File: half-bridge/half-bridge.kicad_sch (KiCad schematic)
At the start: 97 parts, among them J1 Conn_01x11_Pin, J3 Conn_01x11_Pin, J4 Conn_01x11_Pin, J5 Conn_01x11_Pin, J6 Conn_01x11_Pin, Q1 EPC2306, Q2 EPC2306, U1 LMG1210, U2 INA293B

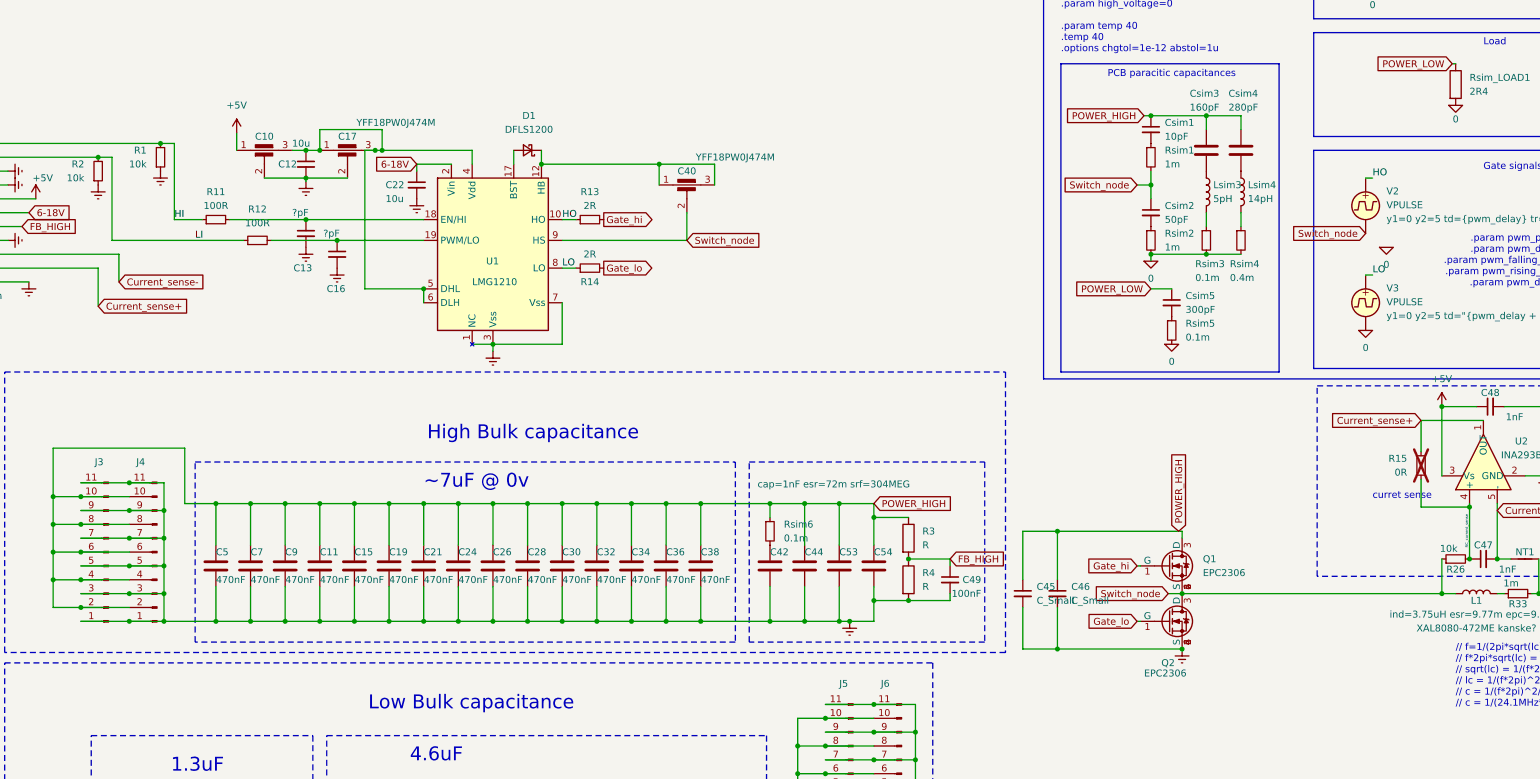
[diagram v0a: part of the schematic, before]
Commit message: Try to move closer to what EPC calls 'Optimal layout'
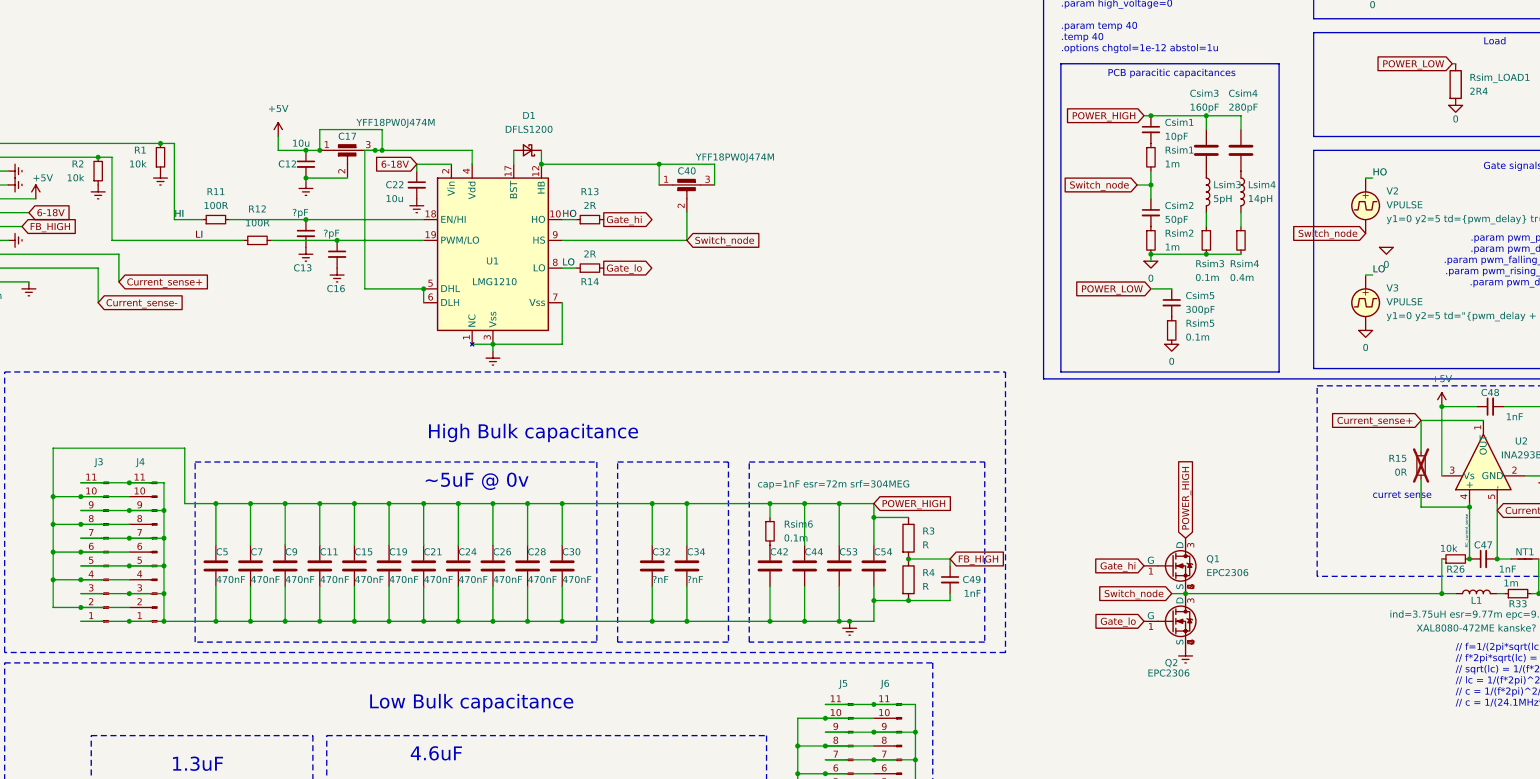
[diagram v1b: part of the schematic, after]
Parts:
- removed C10: YFF18PW0J474M, Library:C_0603_1608Metric_Feedthrough_W_Vias, symbol Device:C_Feedthrough
- removed C36, C38: 470nF, Capacitor_SMD:C_1210_3225Metric, symbol Device:C
- removed C45, C46: C_Small, Capacitor_SMD:C_0603_1608Metric, symbol Device:C_Small
- C32, C34: value 470nF -> ?nF; footprint Capacitor_SMD:C_1210_3225Metric -> Capacitor_SMD:C_0805_2012Metric
- C49: value 100nF -> 1nF
- R3: footprint (none) -> Resistor_SMD:R_1206_3216Metric
- R33: now left out of the parts list
- R4: footprint (none) -> Resistor_SMD:R_0805_2012Metric
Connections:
- net +5V: now also C12.1, C17.1, C17.3, U1.4 (Vdd), U1.5 (DHL), U1.6 (DLH)
- net Current_sense+: now also J1.3 (Pin_3); no longer J1.2 (Pin_2)
- net Current_sense-: now also J1.2 (Pin_2); no longer J1.3 (Pin_3)
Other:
- note added: "~5uF @ 0v"
- note removed: "~7uF @ 0v"
- moved on the sheet: C32, C34, Q1, Q2

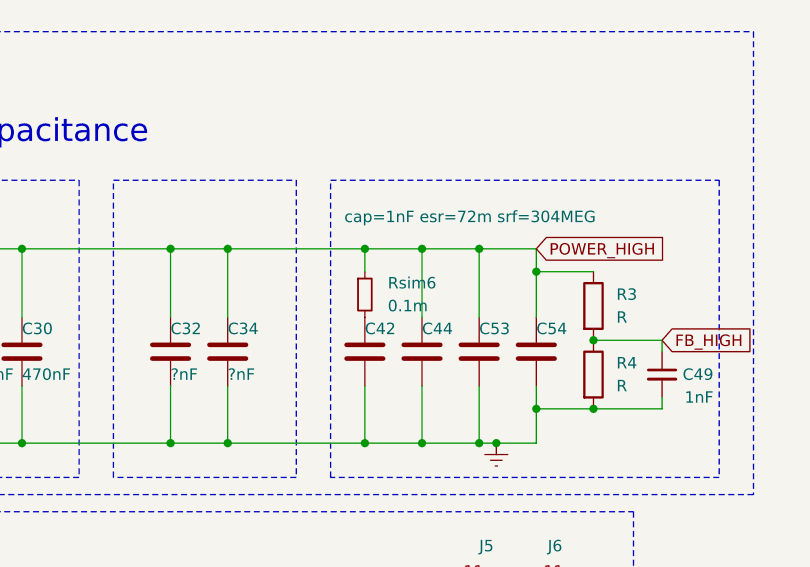
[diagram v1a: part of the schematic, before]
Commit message: Further layout improvements
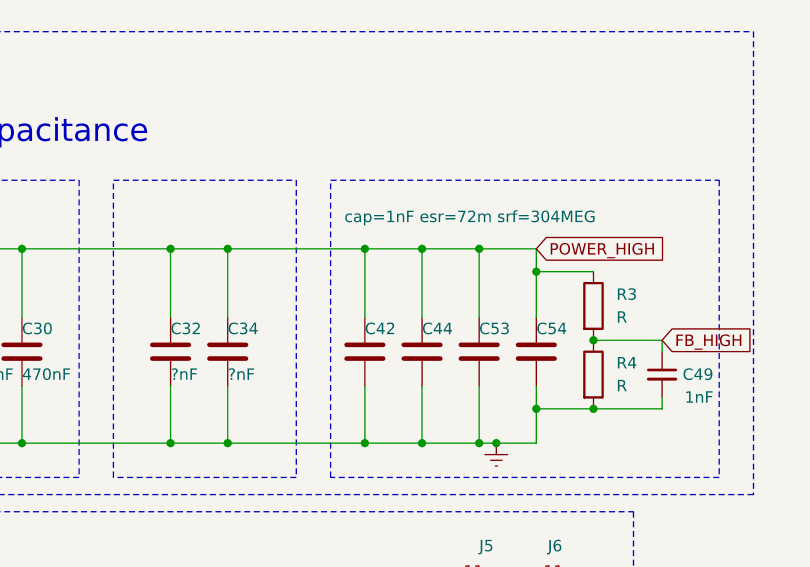
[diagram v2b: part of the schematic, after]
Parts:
- removed Rsim6: 0.1m, symbol Device:R_Small
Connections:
- net POWER_HIGH: now also C42.1
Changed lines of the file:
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@@
 	(wire
 		(pts
+			(xy 175.26 142.24) (xy 175.26 149.86)
+		)
+		(stroke
+			(width 0)
+			(type default)
+		)
+	)
+	(wire
+		(pts
 			(xy 180.34 201.93) (xy 185.42 201.93)
 		)
@@
 	(wire
 		(pts
-			(xy 175.26 142.24) (xy 175.26 144.78)
-		)
-		(stroke
-			(width 0)
-			(type default)
-		)
-	)
-	(wire
-		(pts
 			(xy 200.66 160.02) (xy 208.28 160.02)
 		)
@@
 					(unit 1)
 				)
-			)
-		)
-	)
-	(symbol
-		(lib_id "Device:R_Small")
-		(at 175.26 147.32 0)
-		(unit 1)
-		(exclude_from_sim no)
-		(in_bom no)
-		(on_board no)
-		(dnp no)
-		(fields_autoplaced yes)
-		(property "Reference" "Rsim6"
-			(at 177.8 146.0499 0)
-			(effects
-				(font
-					(size 1.27 1.27)
-				)
-				(justify left)
-			)
-		)
-		(property "Value" "0.1m"
-			(at 177.8 148.5899 0)
-			(effects
-				(font
-					(size 1.27 1.27)
-				)
-				(justify left)
-			)
-		)
-		(property "Footprint" ""
-			(at 175.26 147.32 0)
-			(effects
-				(font
-					(size 1.27 1.27)
-				)
-				(hide yes)
-			)
-		)
-		(property "Datasheet" "~"
-			(at 175.26 147.32 0)
-			(effects
-				(font
-					(size 1.27 1.27)
-				)
-				(hide yes)
-			)
-		)
-		(property "Description" "Resistor, small symbol"
-			(at 175.26 147.32 0)
-			(effects
-				(font
-					(size 1.27 1.27)
-				)
-				(hide yes)
-			)
-		)
-		(property "Sim.Device" "R"
-			(at 175.26 147.32 0)
-			(effects
-				(font
-					(size 1.27 1.27)
-				)
-				(hide yes)
-			)
-		)
-		(property "Sim.Pins" "1=+ 2=-"
-			(at 175.26 147.32 0)
-			(effects
-				(font
-					(size 1.27 1.27)
-				)
-				(hide yes)
-			)
-		)
-		(pin "2"
-		)
-		(pin "1"
-		)
-		(instances
-			(project "half-bridge"
-				(path "/561c49c4-2e8b-46fe-9ff5-6f6657079a69"
-					(reference "Rsim6")
-					(unit 1)
-				)

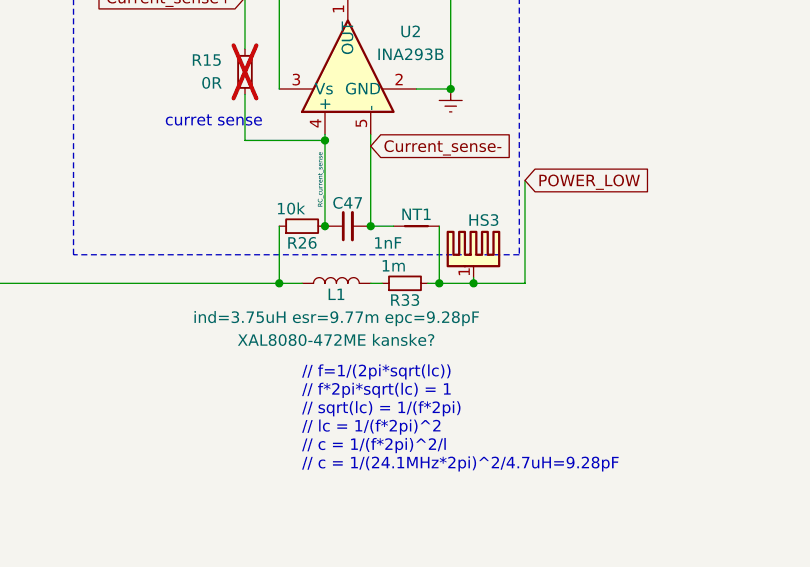
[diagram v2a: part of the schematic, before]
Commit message: Clean up overlapping vias and zones
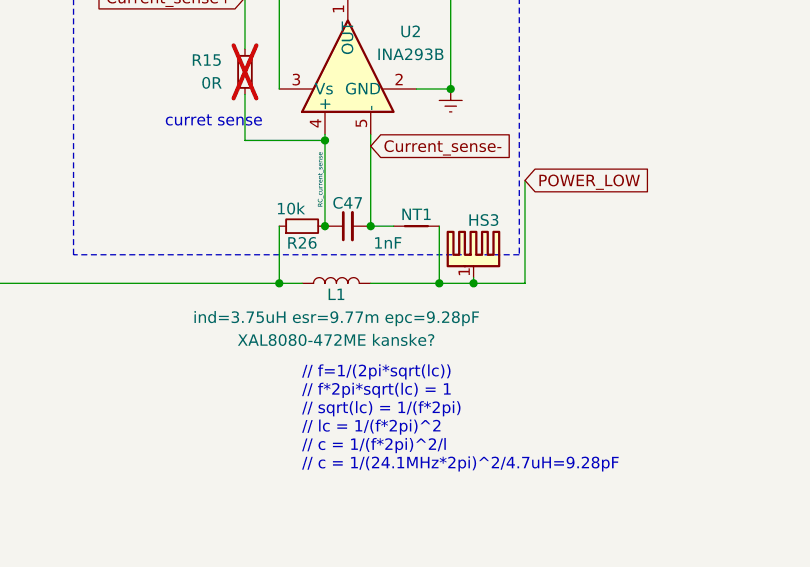
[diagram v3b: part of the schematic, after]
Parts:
- removed R33: 1m, Resistor_SMD:R_1206_3216Metric, symbol Device:R_Small
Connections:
- net POWER_LOW: now also L1.2
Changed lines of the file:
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@@
 	(wire
 		(pts
-			(xy 309.88 158.75) (xy 308.61 158.75)
+			(xy 308.61 158.75) (xy 316.23 158.75)
 		)
 		(stroke
@@
 	(wire
 		(pts
-			(xy 314.96 158.75) (xy 316.23 158.75)
-		)
-		(stroke
-			(width 0)
-			(type default)
-		)
-	)
-	(wire
-		(pts
 			(xy 66.675 194.31) (xy 73.025 194.31)
 		)
@@
 					(unit 1)
 				)
-			)
-		)
-	)
-	(symbol
-		(lib_id "Device:R_Small")
-		(at 312.42 158.75 90)
-		(unit 1)
-		(exclude_from_sim no)
-		(in_bom no)
-		(on_board no)
-		(dnp no)
-		(property "Reference" "R33"
-			(at 312.42 160.655 90)
-			(effects
-				(font
-					(size 1.27 1.27)
-				)
-			)
-		)
-		(property "Value" "1m"
-			(at 311.15 156.845 90)
-			(effects
-				(font
-					(size 1.27 1.27)
-				)
-			)
-		)
-		(property "Footprint" "Resistor_SMD:R_1206_3216Metric"
-			(at 312.42 158.75 0)
-			(effects
-				(font
-					(size 1.27 1.27)
-				)
-				(hide yes)
-			)
-		)
-		(property "Datasheet" "~"
-			(at 312.42 158.75 0)
-			(effects
-				(font
-					(size 1.27 1.27)
-				)
-				(hide yes)
-			)
-		)
-		(property "Description" ""
-			(at 312.42 158.75 0)
-			(effects
-				(font
-					(size 1.27 1.27)
-				)
-				(hide yes)
-			)
-		)
-		(pin "1"
-		)
-		(pin "2"
-		)
-		(instances
-			(project "half-bridge"
-				(path "/561c49c4-2e8b-46fe-9ff5-6f6657079a69"
-					(reference "R33")
-					(unit 1)
-				)

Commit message: More changes
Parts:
- removed C1, C2, C3, C4, C6, C8: 220nF, Capacitor_SMD:C_1206_3216Metric, symbol Device:C
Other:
- note removed: "1.3uF"

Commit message: More changes
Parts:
- added H1, H2, H3, H4, H5: WE 97730256330, Mounting_Wuerth:Mounting_Wuerth_WA-SMSI-M1.6_H2.5mm_ThreadDepth1.5mm_NoNPTH_97730256330, symbol Mechanical:MountingHole_Pad
- added J2, J7, J8, J9: MountingHole_Pad, Connector_Wire:SolderWirePad_1x01_SMD_5x10mm, symbol Mechanical:MountingHole_Pad
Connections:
- net 0: now also H1.1, H3.1, H4.1, J2.1, J8.1
- net POWER_HIGH: now also H2.1, J7.1
- net POWER_LOW: now also H5.1, J9.1
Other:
- note added: "Heat sink mounting holes"

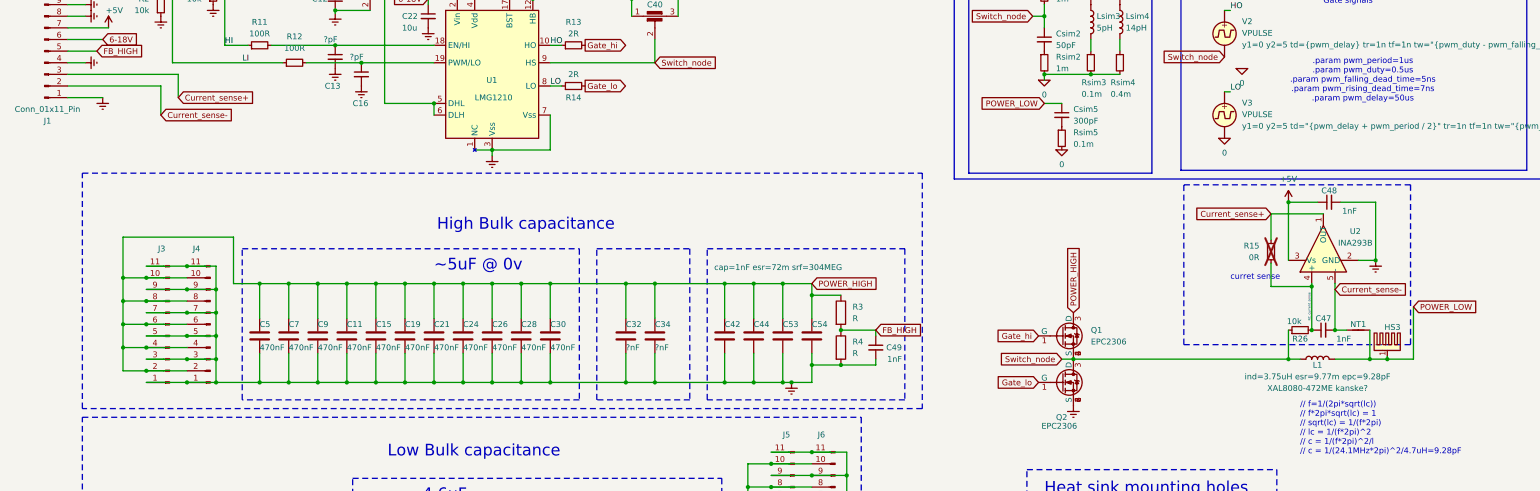
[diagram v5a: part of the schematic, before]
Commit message: Add some more small cap
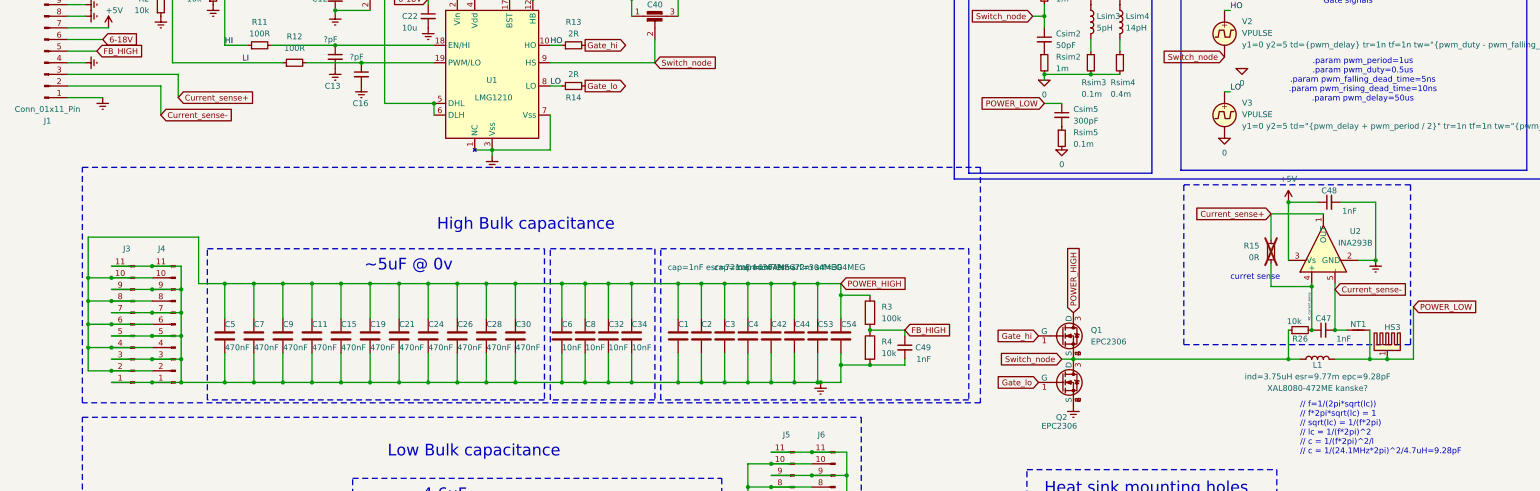
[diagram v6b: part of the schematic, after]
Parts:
- added C1, C2, C3, C4: ${SIM.PARAMS}, Capacitor_SMD:C_0402_1005Metric, symbol Device:C
- added C6, C8: 10nF, Capacitor_SMD:C_0805_2012Metric, symbol Device:C
- C32, C34: value ?nF -> 10nF
- R3: value R -> 100k
- R4: value R -> 10k
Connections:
- net 0: now also C1.2, C2.2, C3.2, C4.2, C6.2, C8.2
- net POWER_HIGH: now also C1.1, C2.1, C3.1, C4.1, C6.1, C8.1
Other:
- note added: ".param pwm_period=1us .param pwm_duty=0.5us .param pwm_falling_dead_time=5ns .param pwm_rising_dead_time=10ns .param pwm_delay=50us"
- note removed: ".param pwm_period=1us .param pwm_duty=0.5us .param pwm_falling_dead_time=5ns .param pwm_rising_dead_time=7ns .param pwm_delay=50us"
- moved on the sheet: C11, C15, C19, C21, C24, C26, C28, C30, C32, C34, C42, C44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

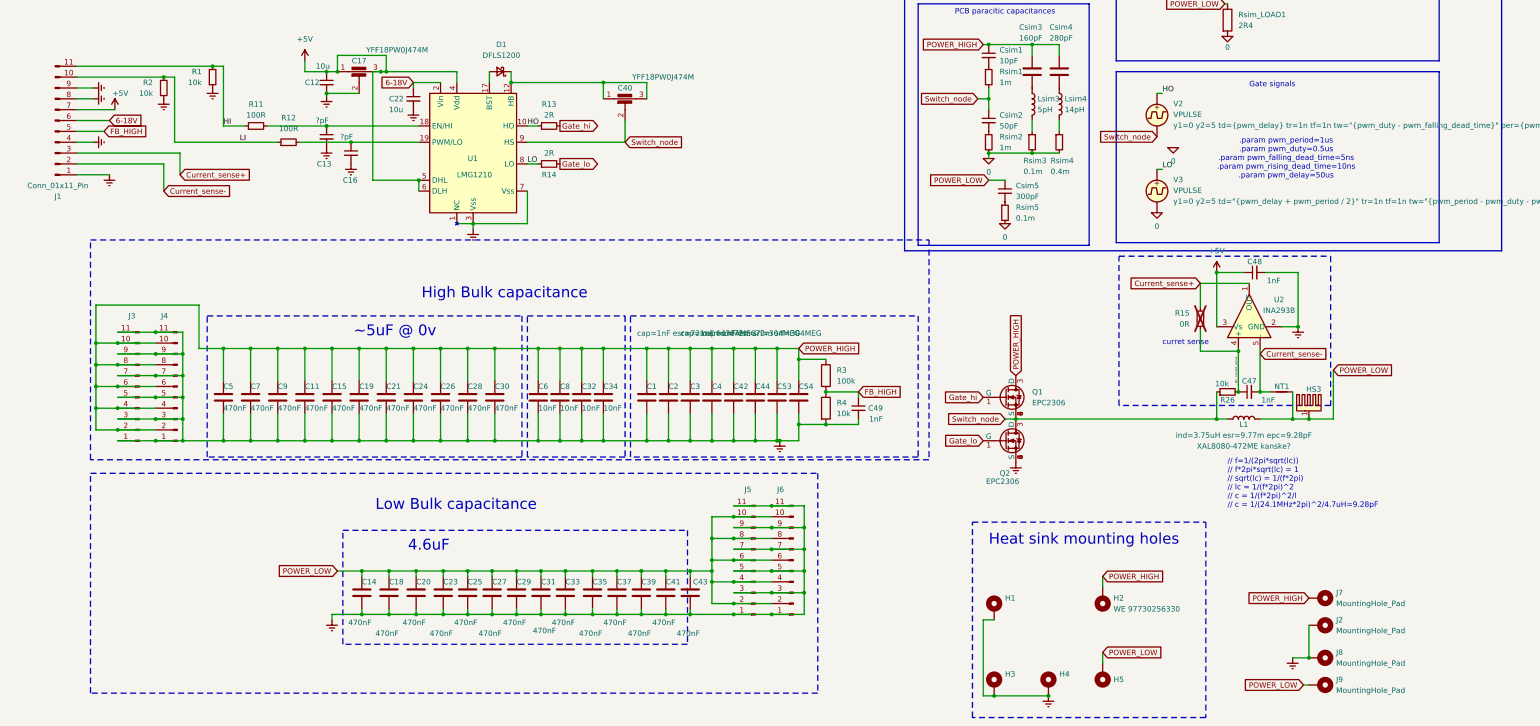
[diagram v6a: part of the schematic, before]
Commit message: Add NTC
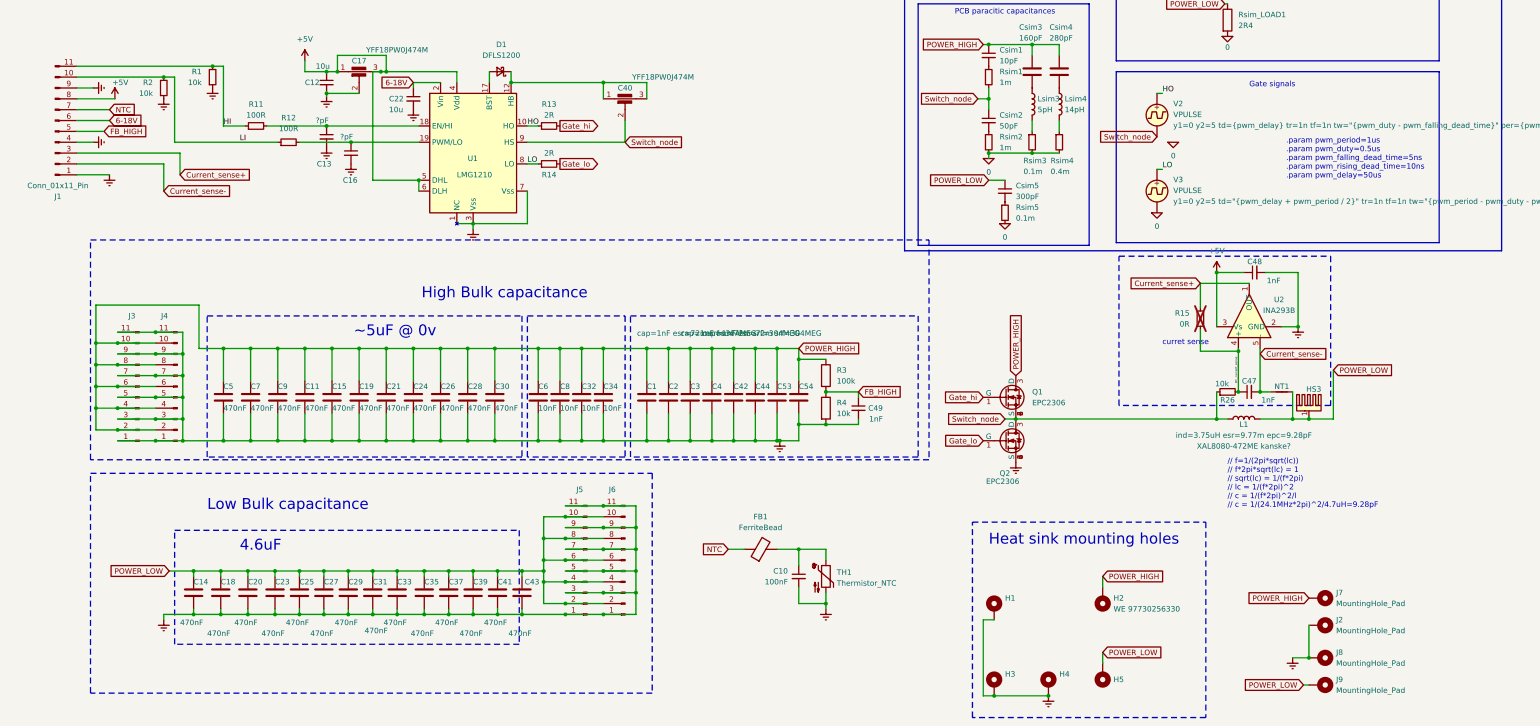
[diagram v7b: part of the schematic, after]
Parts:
- added C10: 100nF, Capacitor_SMD:C_0402_1005Metric, symbol Device:C_Small
- added FB1: FerriteBead, Inductor_SMD:L_0603_1608Metric, symbol Device:FerriteBead
- added TH1: Thermistor_NTC, Resistor_SMD:R_0603_1608Metric, symbol Device:Thermistor_NTC
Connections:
- net +5V: now also J1.8 (Pin_8); no longer J1.7 (Pin_7)
- net 0: now also C10.2, TH1.2; no longer J1.8 (Pin_8)
- new net: C10.1, FB1.2, TH1.1
- new net NTC: FB1.1, J1.7 (Pin_7)
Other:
- moved on the sheet: C14, C18, C20, C23, C25, C27, C29, C31, C33, C35, C37, C39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
